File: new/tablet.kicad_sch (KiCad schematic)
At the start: 17 parts, among them J1 FSMC/TOUCH-SPI, J2 USB_B_Micro, J3 SD/CARD, J4 FLASH/FONT, U1 STM32F429Z_E-G_Tx

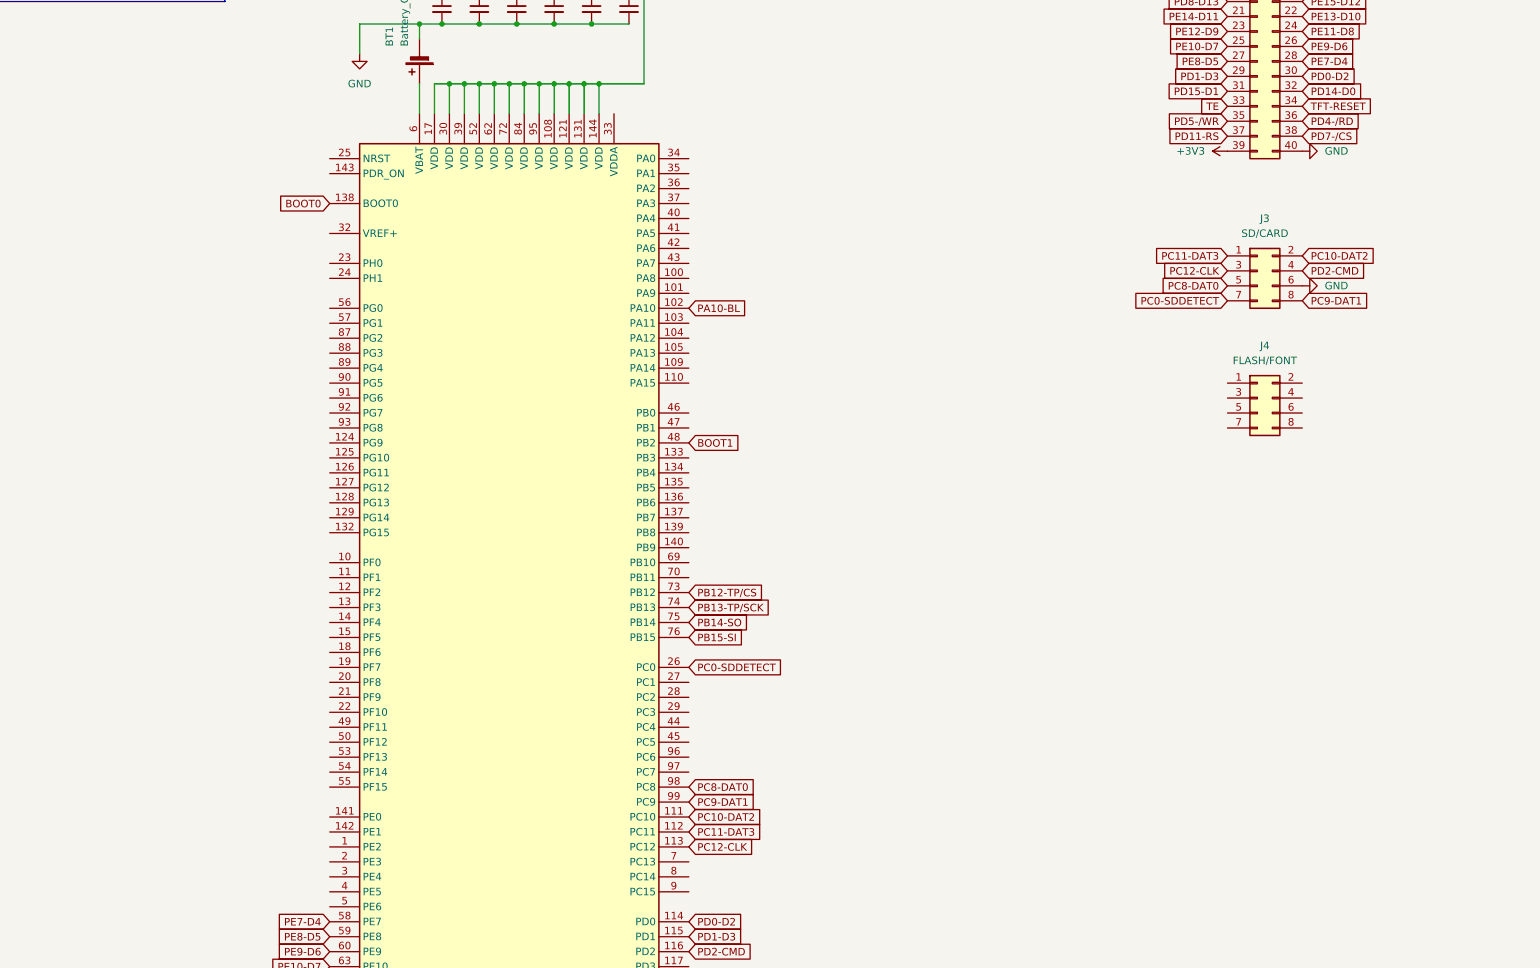
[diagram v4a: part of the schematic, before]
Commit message: add TPS63001
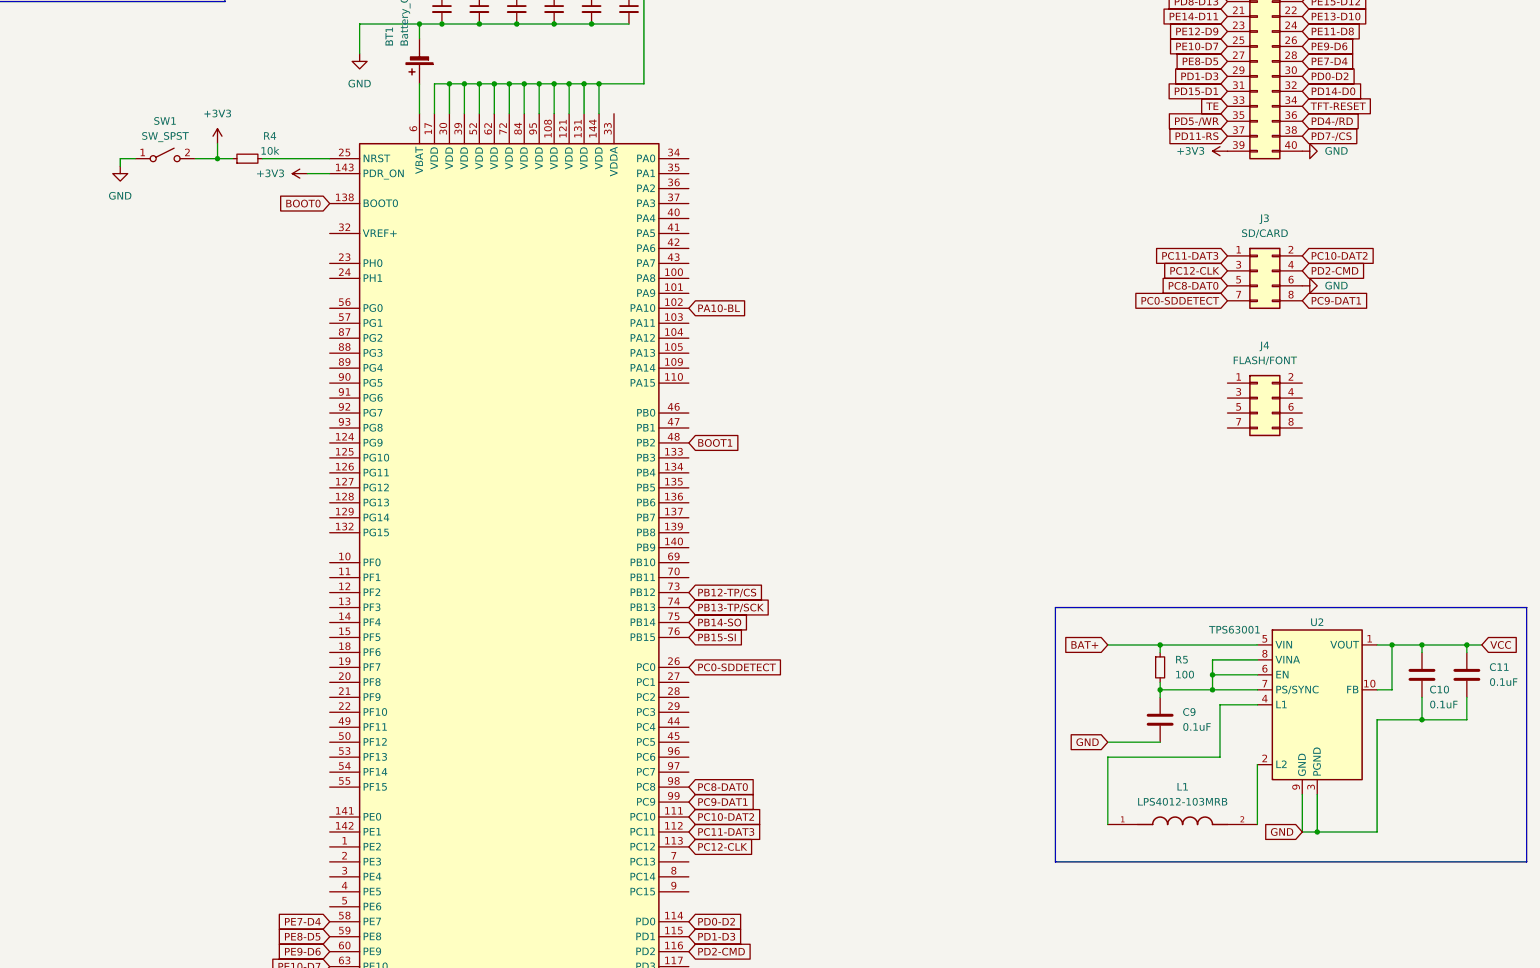
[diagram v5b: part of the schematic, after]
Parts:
- added C10, C11, C9: 0.1uF, Capacitor_SMD:C_0603_1608Metric, symbol Device:C
- added L1: LPS4012-103MRB, Inductor_SMD:L_Sunlord_SWPA4012S, symbol LPS4012:LPS4012-103MRB
- added R4: 10k, Resistor_SMD:R_0603_1608Metric, symbol Device:R_Small
- added R5: 100, Resistor_SMD:R_0603_1608Metric, symbol Device:R_Small
- added SW1: SW_SPST, Button_Switch_SMD:SW_SPST_CK_RS282G05A3, symbol Switch:SW_SPST
- added U2: TPS63001, Package_SON:Texas_DRC0010J_ThermalVias, symbol Regulator_Switching:TPS63000
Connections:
- net +3V3: now also U1.143 (PDR_ON), R4.1, SW1.2 (B)
- net GND: now also C10.2, C11.2, C9.2, SW1.1 (A), U2.11 (PGND), U2.3 (PGND), U2.9 (GND)
- net at U1.25 (NRST): now also R4.2
- new net: C9.1, R5.2, U2.6 (EN), U2.7 (PS/SYNC), U2.8 (VINA)
- new net: L1.1, U2.4 (L1)
- new net: L1.2, U2.2 (L2)
- new net BAT+: R5.1, U2.5 (VIN)
- new net VCC: C10.1, C11.1, U2.1 (VOUT), U2.10 (FB)

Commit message: add wiring + battery charging
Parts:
- added C12, C13: 0.1uF, Capacitor_SMD:C_0603_1608Metric, symbol Device:C
- added C14, C15: 0.1uF, Capacitor_SMD:C_0603_1608Metric, symbol Device:C_Small
- added D1: BAT48JFILM, Diode_SMD:D_SOD-323, symbol Diode:BAT48JFILM
- added D2: LED_Small, Resistor_SMD:R_0603_1608Metric, symbol Device:LED_Small
- added J5: Conn_02x03_Odd_Even, Connector_PinHeader_2.54mm:PinHeader_2x03_P2.54mm_Vertical_SMD, symbol Connector_Generic:Conn_02x03_Odd_Even
- added J6: Conn_01x02, Connector_PinSocket_2.54mm:PinSocket_1x02_P2.54mm_Vertical, symbol Connector_Generic:Conn_01x02
- added Q1: DMG2301L, Package_TO_SOT_SMD:SOT-23, symbol Transistor_FET:DMG2301L
- added R10, R6, R7, R8, R9: 10k, Resistor_SMD:R_0603_1608Metric, symbol Device:R_Small
- added R11, R12: 2k, Resistor_SMD:R_0603_1608Metric, symbol Device:R_Small
- added TP1: VIN, Connector_Wire:SolderWirePad_1x01_SMD_1x2mm, symbol Connector:TestPoint
- added U3: MCP73811T-420I-OT, Package_TO_SOT_SMD:SOT-23-5, symbol Battery_Management:MCP73811T-420I-OT
- added Y1: Crystal, Crystal:Crystal_SMD_HC49-SD, symbol Device:Crystal
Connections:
- net VCC is gone; now on net +3V3: C10.1, C11.1, U2.1 (VOUT), U2.10 (FB)
- net +3V3: now also R4.2, R7.1, R9.2; no longer R4.1, SW1.2 (B)
- net BOOT0: now also J5.4 (Pin_4)
- net BOOT1: now also J5.3 (Pin_3)
- net GND: now also C12.2, C13.2, C14.2, C15.2, J6.2 (Pin_2), R10.1, R11.2, R6.2, R8.1, U3.2 (V_{SS})
- net PA11: now also U1.103 (PA11)
- net PA12: now also U1.104 (PA12)
- net at U1.25 (NRST): now also R4.1, SW1.2 (B); no longer R4.2
- net PH0: now reaches U1.23 (PH0)
- net PH0: now also C15.1, Y1.2
- net PH1: now reaches U1.24 (PH1)
- net PH1: now also C14.1, Y1.1
- net +5V renamed VBUS
- net VBUS: now also C13.1, D1.2 (A), D2.2 (A), Q1.1 (G), R10.2, U3.4 (V_{DD})
- net BAT+: no longer names the net of R5.1, U2.5 (VIN)
- net BAT+: now also D1.1 (K), Q1.2 (S), TP1.1
- new net: R11.1, U3.5 (PROG)
- new net: J5.6 (Pin_6), R8.2
- new net: J5.2 (Pin_2), R9.1
- new net: J5.5 (Pin_5), R6.1
- new net: J5.1 (Pin_1), R7.2
- new net: R12.2, U3.1 (CE)
- new net: D2.1 (K), R12.1
- new net +BATT: C12.1, J6.1 (Pin_1), Q1.3 (D), U3.3 (V_{BAT})
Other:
- moved on the sheet: C10, C11, C9, L1, R4, R5, SW1, U2

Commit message: wiring
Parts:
- added J7: Conn_ARM_SWD_TagConnect_TC2030, Connector_PinHeader_2.54mm:PinHeader_1x06_P2.54mm_Vertical, symbol Connector:Conn_ARM_SWD_TagConnect_TC2030
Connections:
- net +3V3: now also J7.1 (VCC)
- net GND: now also J7.5 (GND)
- net RESET: now reaches R4.1, SW1.2 (B), U1.25 (NRST)
- net RESET: now also J7.3 (~{RESET})
- net PA13-SWDIO: now reaches U1.105 (PA13)
- net PA13-SWDIO: now also J7.2 (SWDIO)
- net PA14-SWCLK: now reaches U1.109 (PA14)
- net PA14-SWCLK: now also J7.4 (SWCLK)
- net PB3-SWO: now reaches U1.133 (PB3)
- net PB3-SWO: now also J7.6 (SWO)
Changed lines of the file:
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@@
   (junction (at 336.55 53.34) (diameter 0) (color 0 0 0 0)
   )
+  (junction (at 76.2 80.01) (diameter 0) (color 0 0 0 0)
+  )
   (junction (at 116.84 52.07) (diameter 0) (color 0 0 0 0)
   )
@@
     (stroke (width 0) (type default))
   )
+  (wire (pts (xy 76.2 80.01) (xy 78.74 80.01))
+    (stroke (width 0) (type default))
+  )
   (wire (pts (xy 347.98 73.66) (xy 347.98 83.82))
     (stroke (width 0) (type default))
@@
     (stroke (width 0) (type default))
   )
-  (wire (pts (xy 72.39 80.01) (xy 78.74 80.01))
+  (wire (pts (xy 72.39 80.01) (xy 76.2 80.01))
     (stroke (width 0) (type default))
   )
@@
   )
   (wire (pts (xy 341.63 72.39) (xy 341.63 63.5))
+    (stroke (width 0) (type default))
+  )
+  (wire (pts (xy 76.2 78.74) (xy 76.2 80.01))
     (stroke (width 0) (type default))
   )
@@
     )
   )
+  (global_label "PA13-SWDIO" (shape input) (at 139.7 113.03 0) (fields_autoplaced)
+    (effects (font (size 1.27 1.27)) (justify left))
+    (property "Intersheetrefs" "${INTERSHEET_REFS}" (at 154.9014 113.03 0)
+      (effects (font (size 1.27 1.27)) (justify left) hide)
+    )
+  )
   (global_label "PC10-DAT2" (shape input) (at 243.84 96.52 0) (fields_autoplaced)
     (effects (font (size 1.27 1.27)) (justify left))
@@
     )
   )
+  (global_label "PB3-SWO" (shape input) (at 30.48 78.74 0) (fields_autoplaced)
+    (effects (font (size 1.27 1.27)) (justify left))
+    (property "Intersheetrefs" "${INTERSHEET_REFS}" (at 42.7785 78.74 0)
+      (effects (font (size 1.27 1.27)) (justify left) hide)
+    )
+  )
   (global_label "BOOT1" (shape input) (at 139.7 128.27 0) (fields_autoplaced)
     (effects (font (size 1.27 1.27)) (justify left))
@@
     )
   )
+  (global_label "RESET" (shape input) (at 30.48 68.58 0) (fields_autoplaced)
+    (effects (font (size 1.27 1.27)) (justify left))
+    (property "Intersheetrefs" "${INTERSHEET_REFS}" (at 39.2103 68.58 0)
+      (effects (font (size 1.27 1.27)) (justify left) hide)
+    )
+  )
+  (global_label "PA14-SWCLK" (shape input) (at 139.7 115.57 0) (fields_autoplaced)
+    (effects (font (size 1.27 1.27)) (justify left))
+    (property "Intersheetrefs" "${INTERSHEET_REFS}" (at 155.2642 115.57 0)
+      (effects (font (size 1.27 1.27)) (justify left) hide)
+    )
+  )
   (global_label "PE8-D5" (shape input) (at 78.74 212.09 180) (fields_autoplaced)
     (effects (font (size 1.27 1.27)) (justify right))
@@
     )
   )
+  (global_label "PA14-SWCLK" (shape input) (at 30.48 73.66 0) (fields_autoplaced)
+    (effects (font (size 1.27 1.27)) (justify left))
+    (property "Intersheetrefs" "${INTERSHEET_REFS}" (at 46.0442 73.66 0)
+      (effects (font (size 1.27 1.27)) (justify left) hide)
+    )
+  )
   (global_label "PH1" (shape input) (at 191.77 125.73 90) (fields_autoplaced)
     (effects (font (size 1.27 1.27)) (justify left))
@@
     )
   )
+  (global_label "RESET" (shape input) (at 76.2 78.74 90) (fields_autoplaced)
+    (effects (font (size 1.27 1.27)) (justify left))
+    (property "Intersheetrefs" "${INTERSHEET_REFS}" (at 76.2 70.0097 90)
+      (effects (font (size 1.27 1.27)) (justify left) hide)
+    )
+  )
   (global_label "PD11-RS" (shape input) (at 139.7 237.49 0) (fields_autoplaced)
     (effects (font (size 1.27 1.27)) (justify left))
@@
     )
   )
+  (global_label "PB3-SWO" (shape input) (at 139.7 130.81 0) (fields_autoplaced)
+    (effects (font (size 1.27 1.27)) (justify left))
+    (property "Intersheetrefs" "${INTERSHEET_REFS}" (at 151.9985 130.81 0)
+      (effects (font (size 1.27 1.27)) (justify left) hide)
+    )
+  )
   (global_label "PB12-TP{slash}CS" (shape input) (at 139.7 153.67 0) (fields_autoplaced)
     (effects (font (size 1.27 1.27)) (justify left))
@@
     (property "Intersheetrefs" "${INTERSHEET_REFS}" (at 65.6554 224.79 0)
       (effects (font (size 1.27 1.27)) (justify right) hide)
+    )
+  )
+  (global_label "PA13-SWDIO" (shape input) (at 30.48 76.2 0) (fields_autoplaced)
+    (effects (font (size 1.27 1.27)) (justify left))
+    (property "Intersheetrefs" "${INTERSHEET_REFS}" (at 45.6814 76.2 0)
+      (effects (font (size 1.27 1.27)) (justify left) hide)
     )
   )
@@
     )
   )
+  (symbol (lib_id "power:GND") (at 20.32 83.82 0) (unit 1)
+    (in_bom yes) (on_board yes) (dnp no) (fields_autoplaced)
+    (property "Reference" "#PWR030" (at 20.32 90.17 0)
+      (effects (font (size 1.27 1.27)) hide)
+    )
+    (property "Value" "GND" (at 20.32 88.9 0)
+      (effects (font (size 1.27 1.27)))
+    )
+    (property "Footprint" "" (at 20.32 83.82 0)
+      (effects (font (size 1.27 1.27)) hide)
+    )
+    (property "Datasheet" "" (at 20.32 83.82 0)
+      (effects (font (size 1.27 1.27)) hide)
+    )
+    (pin "1")
+    (instances
+      (project "tablet"
+        (path "/868516f5-1ea3-47ae-b277-3f67998564bb"
+          (reference "#PWR030") (unit 1)
+        )
+      )
+    )
+  )
   (symbol (lib_id "power:+BATT") (at 363.22 110.49 0) (unit 1)
     (in_bom yes) (on_board yes) (dnp no) (fields_autoplaced)
@@
         (path "/868516f5-1ea3-47ae-b277-3f67998564bb"
           (reference "R7") (unit 1)
+        )
+      )
+    )
+  )
+  (symbol (lib_id "power:+3V3") (at 20.32 63.5 0) (unit 1)
+    (in_bom yes) (on_board yes) (dnp no) (fields_autoplaced)
+    (property "Reference" "#PWR029" (at 20.32 67.31 0)
+      (effects (font (size 1.27 1.27)) hide)
+    )
+    (property "Value" "+3V3" (at 20.32 58.42 0)
+      (effects (font (size 1.27 1.27)))
+    )
+    (property "Footprint" "" (at 20.32 63.5 0)
+      (effects (font (size 1.27 1.27)) hide)
+    )
+    (property "Datasheet" "" (at 20.32 63.5 0)
+      (effects (font (size 1.27 1.27)) hide)
+    )
+    (pin "1")
+    (instances
+      (project "tablet"
+        (path "/868516f5-1ea3-47ae-b277-3f67998564bb"
+          (reference "#PWR029") (unit 1)
         )
       )
@@
         )
       )
+    )
+  )
+  (symbol (lib_id "Connector:Conn_ARM_SWD_TagConnect_TC2030") (at 22.86 73.66 0) (unit 1)
+    (in_bom no) (on_board yes) (dnp no) (fields_autoplaced)
+    (property "Reference" "J7" (at 16.51 72.39 0)
+      (effects (font (size 1.27 1.27)) (justify right))
+    )
+    (property "Value" "Conn_ARM_SWD_TagConnect_TC2030" (at 16.51 74.93 0)
+      (effects (font (size 1.27 1.27)) (justify right))
+    )
+    (property "Footprint" "Connector_PinHeader_2.54mm:PinHeader_1x06_P2.54mm_Vertical" (at 22.86 91.44 0)
+      (effects (font (size 1.27 1.27)) hide)
+    )
+    (property "Datasheet" "https://www.tag-connect.com/wp-content/uploads/bsk-pdf-manager/TC2030-CTX_1.pdf" (at 22.86 88.9 0)
+      (effects (font (size 1.27 1.27)) hide)
+    )
+    (pin "1")
+    (pin "2")
+    (pin "3")
+    (pin "4")
+    (pin "5")
+    (pin "6")
+    (instances
+      (project "tablet"
+        (path "/868516f5-1ea3-47ae-b277-3f67998564bb"
+          (reference "J7") (unit 1)
+        )
+      )
